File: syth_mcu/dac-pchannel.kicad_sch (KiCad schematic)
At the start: 23 parts, among them J4 AudioPlug3, Q1 SI2307DS, Q2 SI2304DS, Q3 SI2307DS, Q4 SI2304DS

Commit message: All traces, no drc runs yet
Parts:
- C1, C2: footprint Capacitor_THT:CP_Radial_D4.0mm_P2.00mm -> Capacitor_THT:C_Disc_D5.0mm_W2.5mm_P5.00mm
- C3, C4: footprint Capacitor_THT:C_Disc_D5.0mm_W2.5mm_P2.50mm -> Capacitor_THT:C_Disc_D5.0mm_W2.5mm_P5.00mm
- C5, C7: footprint Capacitor_THT:CP_Radial_D5.0mm_P2.00mm -> Capacitor_THT:C_Disc_D5.0mm_W2.5mm_P5.00mm
- C6, C8: footprint Capacitor_THT:CP_Radial_D4.0mm_P2.00mm -> Capacitor_THT:CP_Radial_D5.0mm_P2.50mm
- J4: footprint synth:CONN-TH_PJ-316 -> synth:TRRS-PJ-320A
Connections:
- net GNDDAC: now also RV6.1, RV7.1; no longer RV6.3, RV7.3
- net at C6.2: now also RV6.3; no longer RV6.1
- net at C8.2: now also RV7.3; no longer RV7.1
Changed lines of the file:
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@@
 			)
 		)
-		(property "Footprint" "synth:CONN-TH_PJ-316"
+		(property "Footprint" "synth:TRRS-PJ-320A"
 			(at 58.42 153.67 0)
 			(hide yes)
@@
 			)
 		)
-		(property "Footprint" "Capacitor_THT:C_Disc_D5.0mm_W2.5mm_P2.50mm"
+		(property "Footprint" "Capacitor_THT:C_Disc_D5.0mm_W2.5mm_P5.00mm"
 			(at 89.8652 46.99 0)
 			(hide yes)
@@
 		(lib_id "Device:R_Potentiometer")
 		(at 104.14 72.39 0)
-		(unit 1)
-		(body_style 1)
-		(exclude_from_sim no)
-		(in_bom yes)
-		(on_board yes)
-		(in_pos_files yes)
-		(dnp no)
-		(fields_autoplaced yes)
+		(mirror x)
+		(unit 1)
+		(body_style 1)
+		(exclude_from_sim no)
+		(in_bom yes)
+		(on_board yes)
+		(in_pos_files yes)
+		(dnp no)
 		(property "Reference" "RV6"
-			(at 101.6 71.1199 0)
+			(at 101.6 73.6601 0)
 			(show_name no)
 			(do_not_autoplace no)
@@
 		)
 		(property "Value" "100k"
-			(at 101.6 73.6599 0)
+			(at 101.6 71.1201 0)
 			(show_name no)
 			(do_not_autoplace no)
@@
 			)
 		)
-		(property "Footprint" "Capacitor_THT:C_Disc_D5.0mm_W2.5mm_P2.50mm"
+		(property "Footprint" "Capacitor_THT:C_Disc_D5.0mm_W2.5mm_P5.00mm"
 			(at 89.8652 102.87 0)
 			(hide yes)
@@
 			)
 		)
-		(property "Footprint" "Capacitor_THT:CP_Radial_D4.0mm_P2.00mm"
+		(property "Footprint" "Capacitor_THT:C_Disc_D5.0mm_W2.5mm_P5.00mm"
 			(at 80.3148 69.85 0)
 			(hide yes)
@@
 		(lib_id "Device:R_Potentiometer")
 		(at 104.14 127 0)
-		(unit 1)
-		(body_style 1)
-		(exclude_from_sim no)
-		(in_bom yes)
-		(on_board yes)
-		(in_pos_files yes)
-		(dnp no)
-		(fields_autoplaced yes)
+		(mirror x)
+		(unit 1)
+		(body_style 1)
+		(exclude_from_sim no)
+		(in_bom yes)
+		(on_board yes)
+		(in_pos_files yes)
+		(dnp no)
 		(property "Reference" "RV7"
-			(at 101.6 125.7299 0)
+			(at 101.6 128.2701 0)
 			(show_name no)
 			(do_not_autoplace no)
@@
 		)
 		(property "Value" "100k"
-			(at 101.6 128.2699 0)
+			(at 101.6 125.7301 0)
 			(show_name no)
 			(do_not_autoplace no)
@@
 			)
 		)
-		(property "Footprint" "Capacitor_THT:CP_Radial_D4.0mm_P2.00mm"
+		(property "Footprint" "Capacitor_THT:C_Disc_D5.0mm_W2.5mm_P5.00mm"
 			(at 80.3148 124.46 0)
 			(hide yes)
@@
 			)
 		)
-		(property "Footprint" "Capacitor_THT:CP_Radial_D4.0mm_P2.00mm"
+		(property "Footprint" "Capacitor_THT:CP_Radial_D5.0mm_P2.50mm"
 			(at 103.1748 120.65 0)
 			(hide yes)
@@
 			)
 		)
-		(property "Footprint" "Capacitor_THT:CP_Radial_D4.0mm_P2.00mm"
+		(property "Footprint" "Capacitor_THT:CP_Radial_D5.0mm_P2.50mm"
 			(at 103.1748 66.04 0)
 			(hide yes)
@@
 			)
 		)
-		(property "Footprint" "Capacitor_THT:CP_Radial_D5.0mm_P2.00mm"
+		(property "Footprint" "Capacitor_THT:C_Disc_D5.0mm_W2.5mm_P5.00mm"
 			(at 105.1052 102.87 0)
 			(hide yes)
@@
 			)
 		)
-		(property "Footprint" "Capacitor_THT:CP_Radial_D5.0mm_P2.00mm"
+		(property "Footprint" "Capacitor_THT:C_Disc_D5.0mm_W2.5mm_P5.00mm"
 			(at 105.1052 46.99 0)
 			(hide yes)

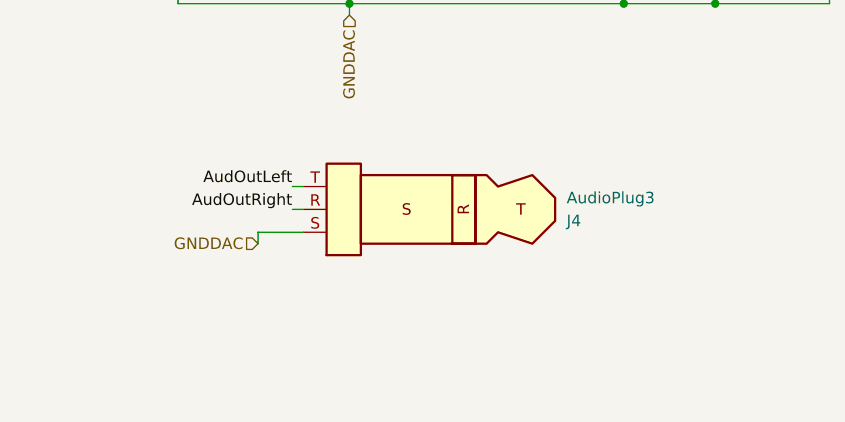
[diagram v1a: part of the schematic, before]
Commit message: pcb: cream bun review fixes (J7 position, Sim.Pins, reformat)
- J7 (1x16 MUX channel socket) moved -2.54mm in x: 154.35->151.81
  (aligns mux channels to hall sensor row)
- dac-pchannel: Sim.Pins corrected on Q1-Q4 + embedded lib defs
  SI2307DS/SI2304DS actual SOT-23 pinout: 1=G 2=S 3=D
  (was 1=D 2=G 3=S per Simulation_SPICE symbol default)
  NOTE: Sim.Pins is SPICE/documentation only — PCB pads still
  routed wrong. Full fix requires schematic symbol swap +
  PCB re-route (GUI work, see open items)
- PB7 I2C trace gap NOT fixed here — requires GUI routing
  (F.Cu gap at bbox 182.26,122.67 -> 191.53,130.30)
- Remaining changes: KiCad auto-reformat from last GUI open

Claude-Session: https://claude.ai/code/session_01VrAYoAfZXAEYgerctdkqLT
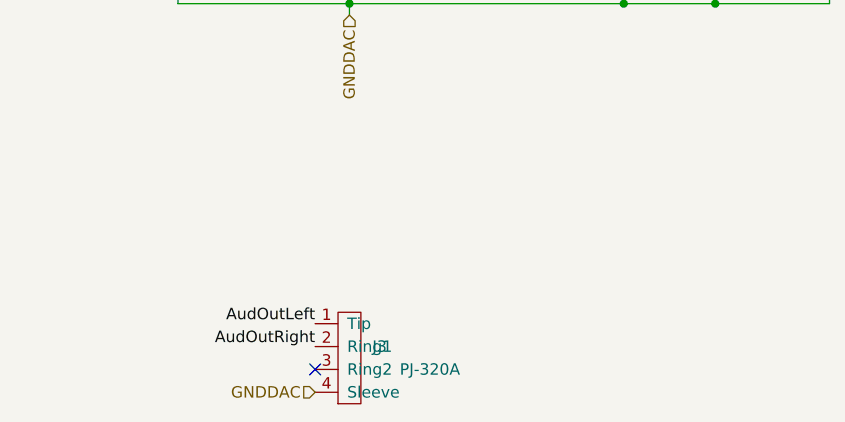
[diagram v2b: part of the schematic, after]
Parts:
- removed J4: AudioPlug3, synth:TRRS-PJ-320A, symbol Connector_Audio:AudioPlug3
- added J3: PJ-320A, synth:TRRS-PJ-320A, symbol synth:PJ-320A
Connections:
- net AudOutLeft: now also J3.1 (Tip)
- net AudOutRight: now also J3.2 (Ring1)
- net GNDDAC: now also J3.4 (Sleeve)
- no-connect marks 0 -> 1
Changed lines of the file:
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@@
 		(color 0 0 0 0)
 	)
+	(no_connect
+		(at 46.99 172.72)
+	)
 	(wire
 		(pts
@@
 	(wire
 		(pts
-			(xy 40.64 158.75) (xy 40.64 157.48)
-		)
-		(stroke
-			(width 0)
-			(type default)
-		)
-	)
-	(wire
-		(pts
-			(xy 40.64 157.48) (xy 45.72 157.48)
-		)
-		(stroke
-			(width 0)
-			(type default)
-		)
-	)
-	(wire
-		(pts
 			(xy 50.8 57.15) (xy 50.8 58.42)
 		)
@@
 	(wire
 		(pts
-			(xy 44.45 152.4) (xy 45.72 152.4)
-		)
-		(stroke
-			(width 0)
-			(type default)
-		)
-	)
-	(wire
-		(pts
 			(xy 81.28 62.23) (xy 81.28 57.15)
 		)
@@
 	(wire
 		(pts
-			(xy 44.45 154.94) (xy 45.72 154.94)
-		)
-		(stroke
-			(width 0)
-			(type default)
-		)
-	)
-	(wire
-		(pts
 			(xy 104.14 46.99) (xy 104.14 48.26)
 		)
@@
 	)
 	(label "AudOutLeft"
-		(at 109.22 127 0)
+		(at 46.99 167.64 180)
 		(effects
 			(font
 				(size 1.27 1.27)
 			)
-			(justify left bottom)
+			(justify right bottom)
 		)
 	)
 	(label "AudOutRight"
-		(at 109.22 72.39 0)
+		(at 46.99 170.18 180)
 		(effects
 			(font
 				(size 1.27 1.27)
 			)
-			(justify left bottom)
+			(justify right bottom)
 		)
 	)
 	(label "AudOutLeft"
-		(at 44.45 152.4 180)
+		(at 109.22 127 0)
 		(effects
 			(font
 				(size 1.27 1.27)
 			)
-			(justify right bottom)
+			(justify left bottom)
 		)
 	)
 	(label "AudOutRight"
-		(at 44.45 154.94 180)
+		(at 109.22 72.39 0)
 		(effects
 			(font
 				(size 1.27 1.27)
 			)
-			(justify right bottom)
+			(justify left bottom)
 		)
 	)
@@
 		)
 	)
-	(hierarchical_label "+3V3 DAC"
+	(hierarchical_label "GNDDAC"
 		(shape input)
-		(at 104.14 91.44 90)
+		(at 46.99 175.26 180)
 		(effects
 			(font
 				(size 1.27 1.27)
 			)
-			(justify left)
+			(justify right)
 		)
 	)
-	(hierarchical_label "DAC Left PWM"
+	(hierarchical_label "+3V3 DAC"
 		(shape input)
-		(at 30.48 111.76 180)
+		(at 104.14 91.44 90)
 		(effects
 			(font
 				(size 1.27 1.27)
 			)
-			(justify right)
+			(justify left)
 		)
 	)
-	(hierarchical_label "GNDDAC"
+	(hierarchical_label "DAC Left PWM"
 		(shape input)
-		(at 50.8 133.35 270)
+		(at 30.48 111.76 180)
 		(effects
 			(font
@@
 	(hierarchical_label "GNDDAC"
 		(shape input)
-		(at 40.64 158.75 180)
+		(at 50.8 133.35 270)
 		(effects
 			(font
@@
 	)
 	(symbol
-		(lib_id "Connector_Audio:AudioPlug3")
-		(at 60.96 154.94 180)
-		(unit 1)
-		(body_style 1)
-		(exclude_from_sim no)
-		(in_bom yes)
-		(on_board yes)
-		(in_pos_files yes)
-		(dnp no)
-		(property "Reference" "J4"
-			(at 74.93 156.2101 0)
-			(show_name no)
-			(do_not_autoplace no)
-			(effects
-				(font
-					(size 1.27 1.27)
-				)
-				(justify right)
-			)
-		)
-		(property "Value" "AudioPlug3"
-			(at 74.93 153.6701 0)
-			(show_name no)
-			(do_not_autoplace no)
-			(effects
-				(font
-					(size 1.27 1.27)
-				)
-				(justify right)
-			)
-		)
-		(property "Footprint" "synth:TRRS-PJ-320A"
-			(at 58.42 153.67 0)
-			(hide yes)
-			(show_name no)
-			(do_not_autoplace no)
-			(effects
-				(font
-					(size 1.27 1.27)
-				)
-			)
-		)
-		(property "Datasheet" ""
-			(at 58.42 153.67 0)
-			(hide yes)
-			(show_name no)
-			(do_not_autoplace no)
-			(effects
-				(font
-					(size 1.27 1.27)
-				)
-			)
-		)
-		(property "Description" "Audio Jack, 3 Poles (Stereo / TRS)"
-			(at 60.96 154.94 0)
-			(hide yes)
-			(show_name no)
-			(do_not_autoplace no)
-			(effects
-				(font
-					(size 1.27 1.27)
-				)
-			)
-		)
-		(pin "T"
-		)
-		(pin "S"
-		)
-		(pin "R"
-		)
-		(instances
-			(project "synth"
-				(path "/1e7814a7-1315-4eb0-a9cb-3b93c6dc7966/1c0b7db5-fb47-467b-b91f-0adacc62fbe2"
-					(reference "J1")
-					(unit 1)
-				)
-			)
-			(project "syth_mcu"
-				(path "/6f6073ad-48fd-4b64-b32f-c8e9bfc21ddc/de801ae6-5eb3-45eb-b018-1b4139932f15"
-					(reference "J4")
-					(unit 1)
-				)
-			)
-		)
-	)
-	(symbol
 		(lib_id "Device:R")
 		(at 31.75 67.31 0)
@@
 			)
 		)
-		(property "Sim.Pins" "1=D 2=G 3=S"
+		(property "Sim.Pins" "1=G 2=S 3=D"
 			(at 48.26 90.17 0)
 			(hide yes)
@@
 	)
 	(symbol
+		(lib_id "synth:PJ-320A")
+		(at 52.07 171.45 0)
+		(unit 1)
+		(body_style 1)
+		(exclude_from_sim no)
+		(in_bom yes)
+		(on_board yes)
+		(in_pos_files yes)
+		(dnp no)
+		(property "Reference" "J3"
+			(at 53.34 170.1799 0)
+			(show_name no)
+			(do_not_autoplace no)
+			(effects
+				(font
+					(size 1.27 1.27)
+				)
+				(justify left)
+			)
+		)
+		(property "Value" "PJ-320A"
+			(at 56.388 172.72 0)
+			(show_name no)
+			(do_not_autoplace no)
+			(effects
+				(font
+					(size 1.27 1.27)
+				)
+				(justify left)
+			)
+		)
+		(property "Footprint" "synth:TRRS-PJ-320A"
+			(at 52.07 171.45 0)
+			(hide yes)
+			(show_name no)
+			(do_not_autoplace no)
+			(effects
+				(font
+					(size 1.27 1.27)
+				)
+			)
+		)
+		(property "Datasheet" ""
+			(at 52.07 171.45 0)
+			(hide yes)
+			(show_name no)
+			(do_not_autoplace no)
+			(effects
+				(font
+					(size 1.27 1.27)
+				)
+			)
+		)
+		(property "Description" "3.5mm Stereo Audio Jack, 4-pin TRRS, PJ-320A"
+			(at 52.07 171.45 0)
+			(hide yes)
+			(show_name no)
+			(do_not_autoplace no)
+			(effects
+				(font
+					(size 1.27 1.27)
+				)
+			)
+		)
+		(pin "2"
+		)
+		(pin "1"
+		)
+		(pin "3"
+		)
+		(pin "4"
+		)
+		(instances
+			(project "syth_mcu"
+				(path "/6f6073ad-48fd-4b64-b32f-c8e9bfc21ddc/de801ae6-5eb3-45eb-b018-1b4139932f15"
+					(reference "J3")
+					(unit 1)
+				)
+			)
+		)
+	)
+	(symbol
 		(lib_id "Device:R")
 		(at 91.44 120.65 0)
@@
 			)
 		)
-		(property "Sim.Pins" "1=D 2=G 3=S"
+		(property "Sim.Pins" "1=G 2=S 3=D"
 			(at 48.26 35.56 0)
 			(hide yes)
@@
 			)
 		)
-		(property "Sim.Pins" "1=D 2=G 3=S"
+		(property "Sim.Pins" "1=G 2=S 3=D"
 			(at 48.26 133.35 0)
 			(hide yes)
@@
 			)
 		)
-		(property "Sim.Pins" "1=D 2=G 3=S"
+		(property "Sim.Pins" "1=G 2=S 3=D"
 			(at 48.26 78.74 0)
 			(hide yes)

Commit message: Fixes from review 2
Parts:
- Q1, Q2, Q3, Q4: footprint Package_TO_SOT_SMD:SOT-23 -> synth:SI230x SOT-23
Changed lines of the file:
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@@
 			)
 		)
-		(property "Footprint" "Package_TO_SOT_SMD:SOT-23"
+		(property "Footprint" "synth:SI230x SOT-23"
 			(at 53.34 107.95 0)
 			(hide yes)
@@
 			)
 		)
-		(property "Footprint" "Package_TO_SOT_SMD:SOT-23"
+		(property "Footprint" "synth:SI230x SOT-23"
 			(at 53.34 53.34 0)
 			(hide yes)
@@
 			)
 		)
-		(property "Footprint" "Package_TO_SOT_SMD:SOT-23"
+		(property "Footprint" "synth:SI230x SOT-23"
 			(at 53.34 115.57 0)
 			(hide yes)
@@
 			)
 		)
-		(property "Footprint" "Package_TO_SOT_SMD:SOT-23"
+		(property "Footprint" "synth:SI230x SOT-23"
 			(at 53.34 60.96 0)
 			(hide yes)

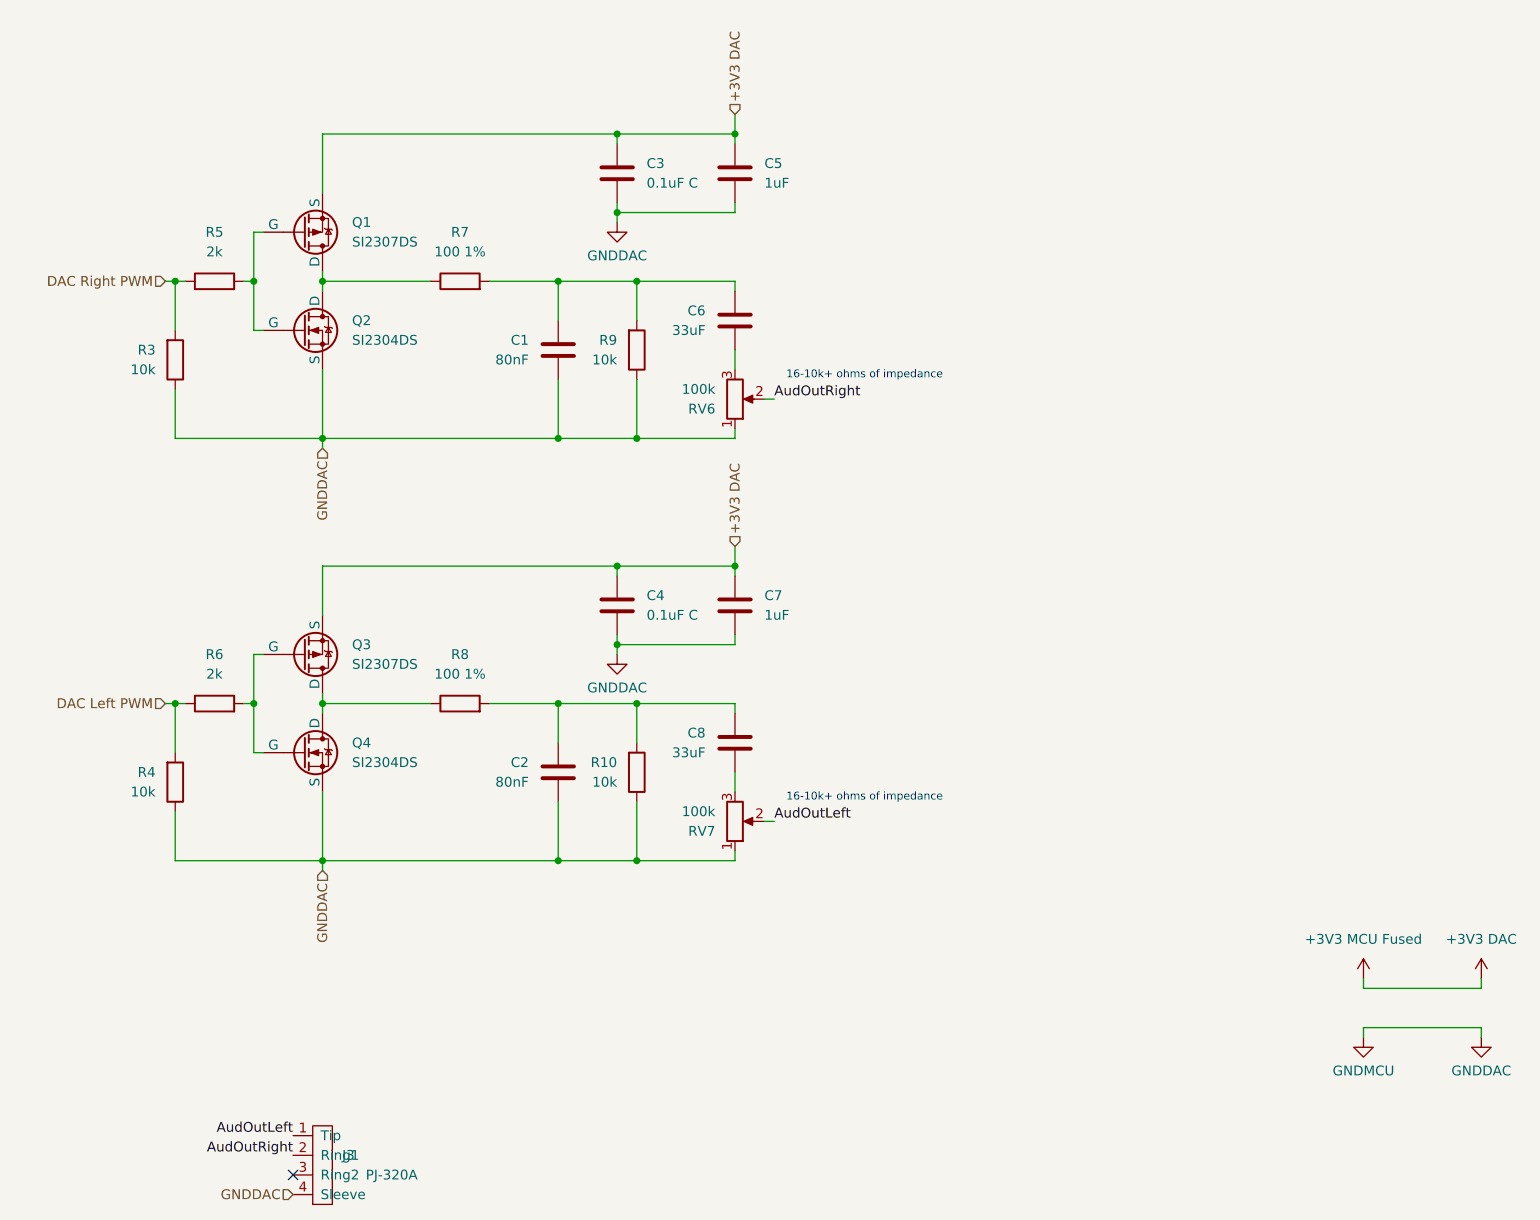
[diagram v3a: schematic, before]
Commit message: Unity-gain audio, merge AMS, 12 pots to mux, revs, footprint
Footprints:
- RXEF fuses with 1x dimension silkscreen and +0.2mm courtyard
- AMS1117 with 0.5mm minimum soldering space on all sides
- SS12D10 wider pins and add courtyard
- Changed orientation of AH3503 TO-92 to match datasheet
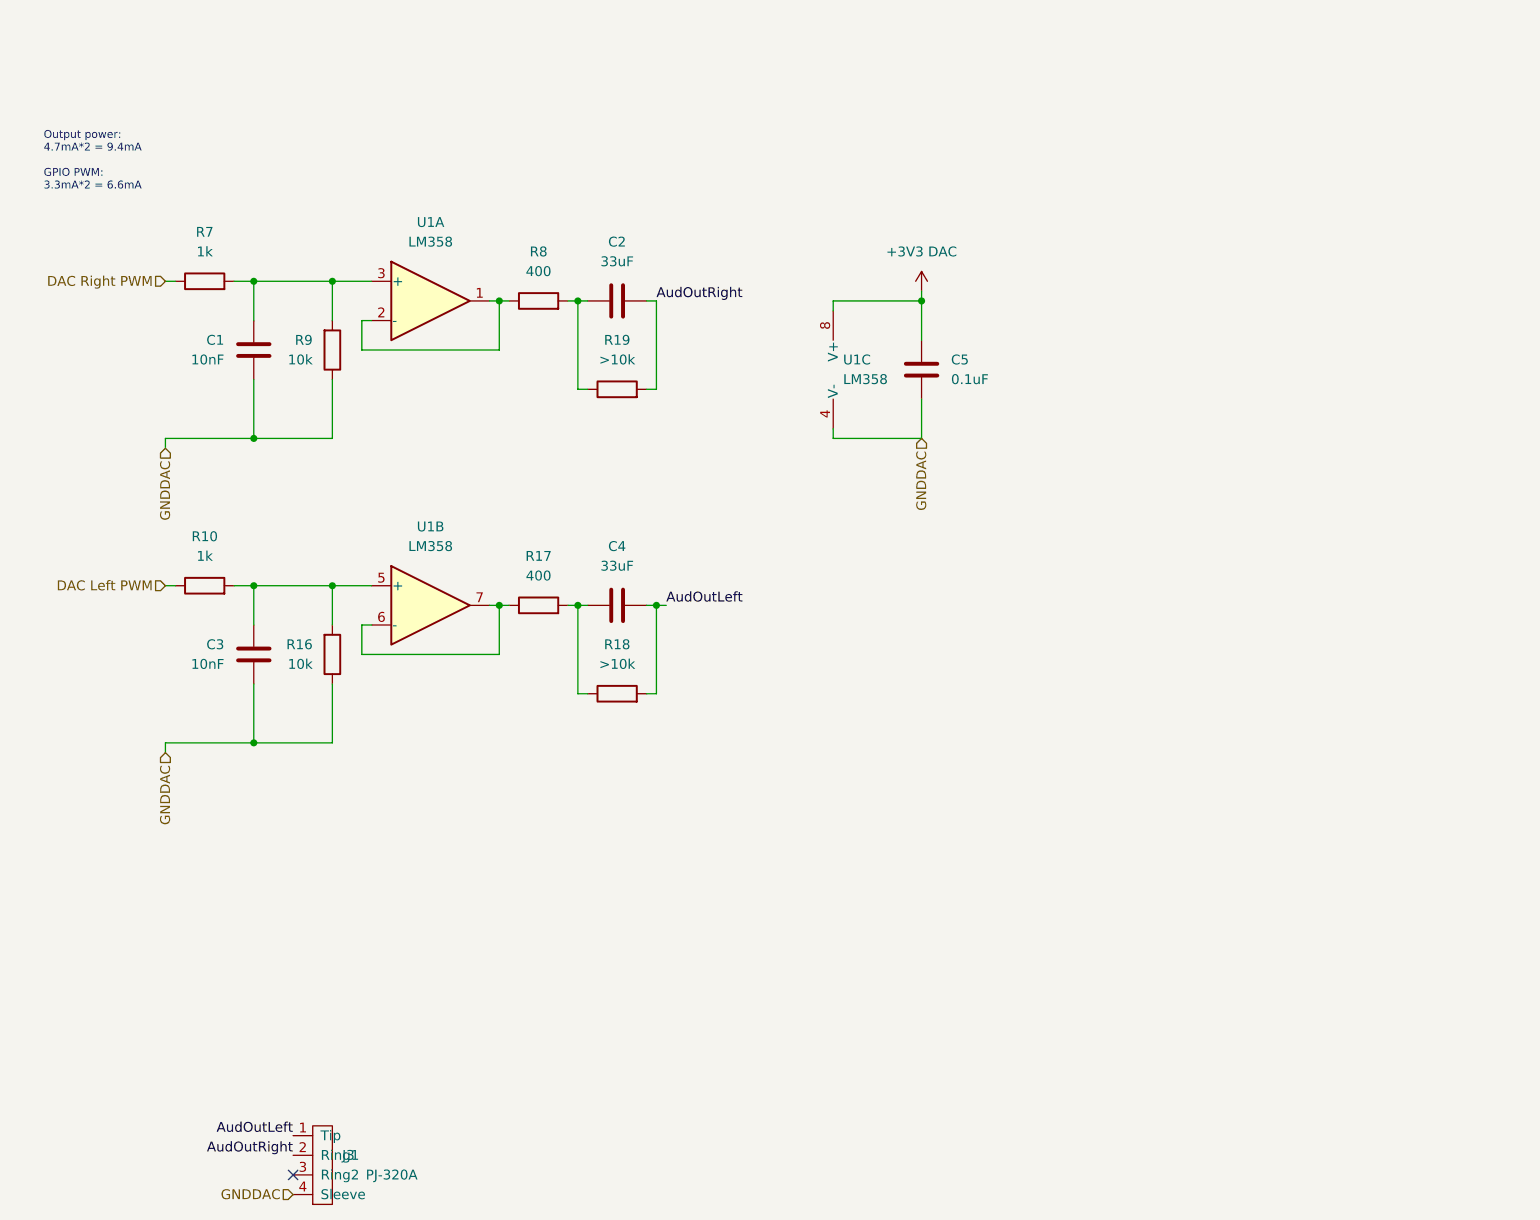
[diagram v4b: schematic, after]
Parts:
- removed C6, C8: 33uF, Capacitor_THT:CP_Radial_D5.0mm_P2.50mm, symbol Device:C
- removed C7: 1uF, Capacitor_THT:C_Disc_D5.0mm_W2.5mm_P5.00mm, symbol Device:C
- removed Q1, Q3: SI2307DS, synth:SI230x SOT-23, symbol Simulation_SPICE:PMOS
- removed Q2, Q4: SI2304DS, synth:SI230x SOT-23, symbol Simulation_SPICE:NMOS
- removed R3, R4: 10k, Resistor_THT:R_Axial_DIN0207_L6.3mm_D2.5mm_P10.16mm_Horizontal, symbol Device:R
- removed R5, R6: 2k, Resistor_THT:R_Axial_DIN0207_L6.3mm_D2.5mm_P10.16mm_Horizontal, symbol Device:R
- removed RV6, RV7: 100k, synth:Potentiometer_Alps_RK09K_Single_Vertical, symbol Device:R_Potentiometer
- added R16: 10k, Resistor_THT:R_Axial_DIN0207_L6.3mm_D2.5mm_P10.16mm_Horizontal, symbol Device:R
- added R17: 400, Resistor_THT:R_Axial_DIN0207_L6.3mm_D2.5mm_P10.16mm_Horizontal, symbol Device:R
- added R18, R19: >10k, Resistor_THT:R_Axial_DIN0207_L6.3mm_D2.5mm_P10.16mm_Horizontal, symbol Device:R
- added U1: LM358, Package_DIP:DIP-8_W7.62mm, symbol Amplifier_Operational:LM358
- C1: value 80nF -> 10nF
- C2: value 80nF -> 33uF; footprint Capacitor_THT:C_Disc_D5.0mm_W2.5mm_P5.00mm -> Capacitor_THT:CP_Radial_D4.0mm_P2.00mm
- C3: value 0.1uF C -> 10nF
- C4: value 0.1uF C -> 33uF; footprint Capacitor_THT:C_Disc_D5.0mm_W2.5mm_P5.00mm -> Capacitor_THT:CP_Radial_D4.0mm_P2.00mm
- C5: value 1uF -> 0.1uF
- R10: value 10k -> 1k
- R7: value 100 1% -> 1k
- R8: value 100 1% -> 400
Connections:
- net +3V3 DAC: now also U1.8 (V+); no longer C3.1, C4.1
- net AudOutLeft: now also C4.2, R18.2
- net AudOutRight: now also C2.2, R19.2
- net DAC Left PWM: now also R10.1
- net DAC Right PWM: now also R7.1
- net GNDDAC: now also R16.1, U1.4 (V-); no longer C2.2, C4.2, R10.1
- net at R8.1: now also U1.1, U1.2 (-)
- net at C2.1, R8.2: now also R19.1; no longer R10.2
- net at C1.1, R7.2, R9.2: now also U1.3 (+)
- new net: C3.1, R10.2, R16.2, U1.5 (+)
- new net: C4.1, R17.2, R18.1
- new net: R17.1, U1.6 (-), U1.7
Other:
- note added: "Output power: 4.7mA*2 = 9.4mA GPIO PWM: 3.3mA*2 = 6.6mA"
- note removed: "16-10k+ ohms of impedance"
- moved on the sheet: C1, R7, R9
